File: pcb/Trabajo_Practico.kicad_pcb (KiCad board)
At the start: 2 copper layers, 64 x 110 mm, 49 parts, among them J1 USB_B_Micro, Q1 UMH3N, SW1 RESET, SW2 SW_SPDT, SW3 UP, SW4 DOWN, SW5 LEFT, SW6 RIGHT, SW7 A, SW8 B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

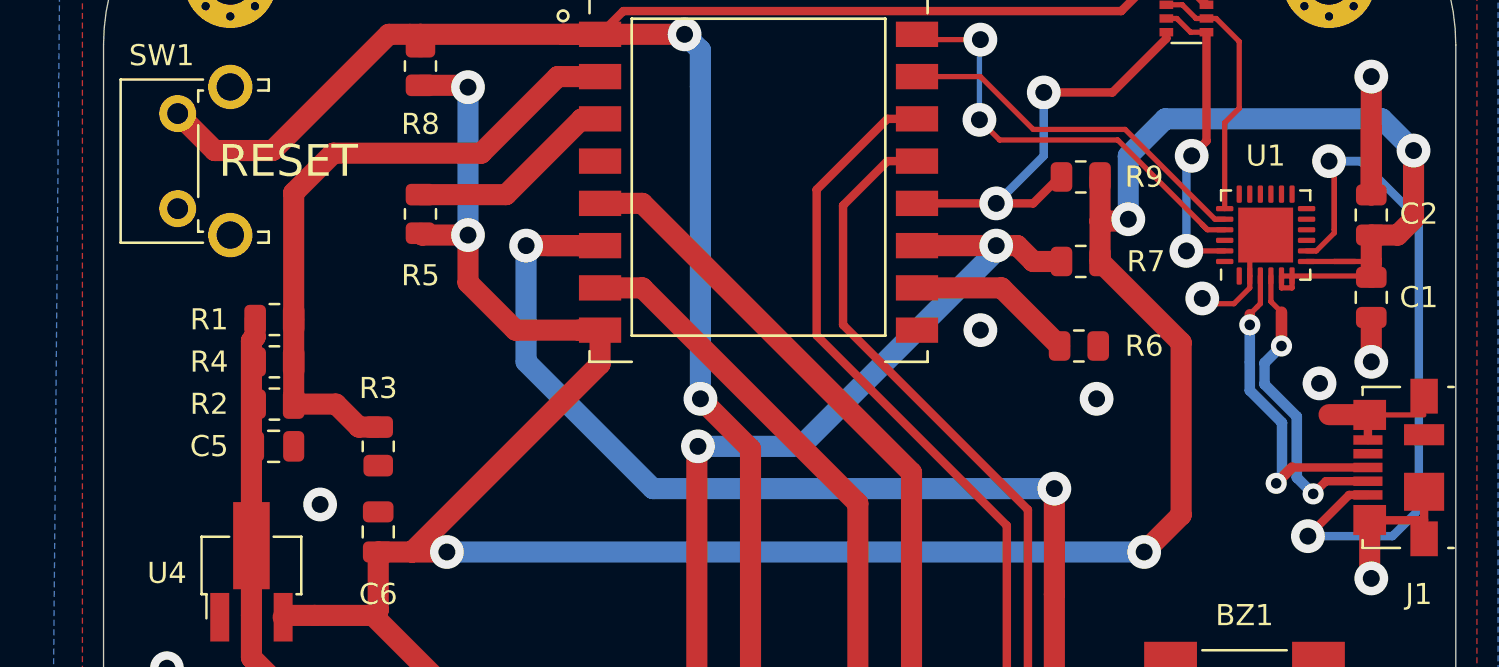
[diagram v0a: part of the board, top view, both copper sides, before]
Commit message: Fix: clearance to 0.25 and values in schematic
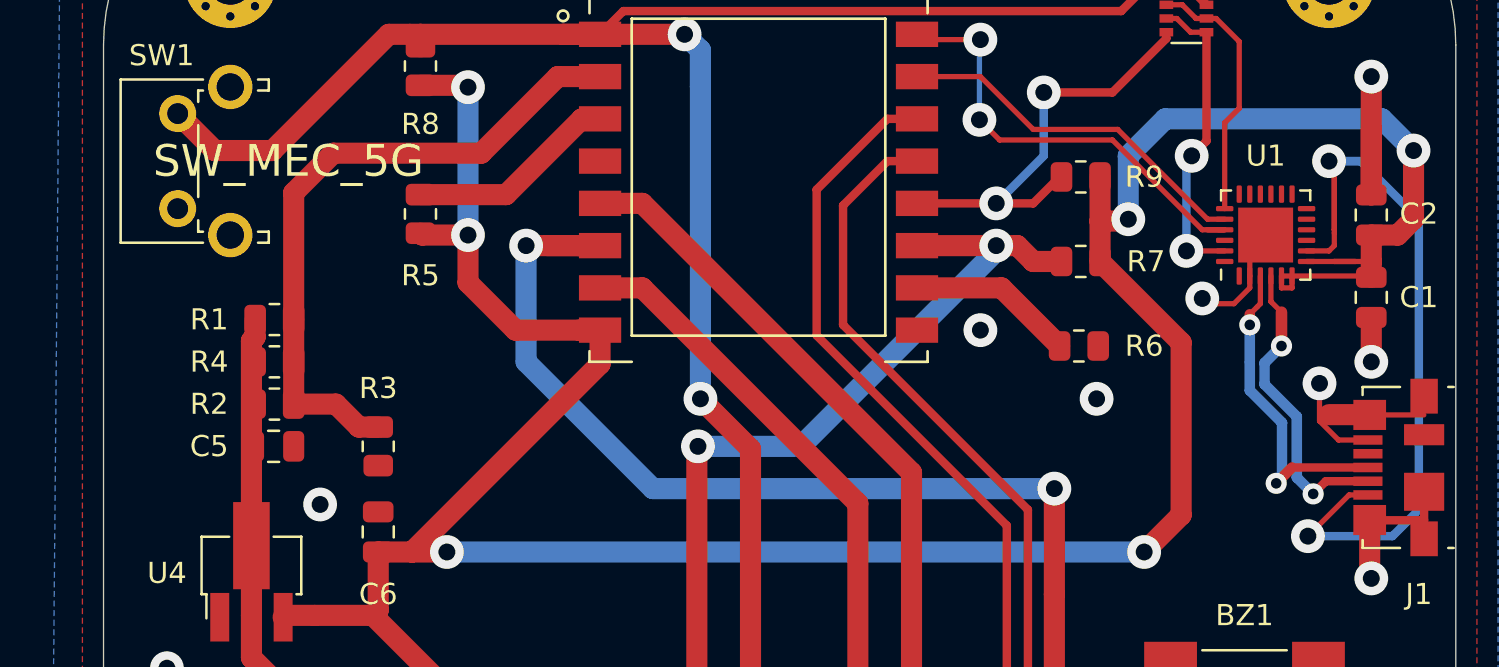
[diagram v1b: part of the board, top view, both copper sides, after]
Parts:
- BZ1: value CMT-8503-85B-SMT-TR -> Buzzer
- DS1: value ST7735_1.44_128x128_SPI -> TFT Display 1.44''
- SW1: value RESET -> SW_MEC_5G
- U1: value CP2104 -> USB2UART
- U3: value PCA9539APW -> GPIO Expander
- U4: value H7650-33PR -> LDO 3.3v 750mA
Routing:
- net GND: track 116.9 -> 120.2 mm
- net /TXD: track 21.0 -> 21.5 mm
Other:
- net class Default: clearance 0.2 -> 0.25
- rule trace_clearance: 0.2 -> 0.25
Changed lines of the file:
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@@
     (thickness 1.6)
     (drawings 37)
-    (tracks 426)
+    (tracks 428)
     (zones 0)
     (modules 49)
@@
     (user_trace_width 0.4)
     (user_trace_width 1)
-    (trace_clearance 0.2)
+    (trace_clearance 0.25)
     (zone_clearance 0.508)
     (zone_45_only no)
@@
   (net 57 /D+)
   (net_class Default "This is the default net class."
-    (clearance 0.2)
+    (clearance 0.25)
     (trace_width 0.4)
     (via_dia 1.6)
@@
       (effects (font (size 1 1) (thickness 0.15)))
     )
-    (fp_text value ST7735_1.44_128x128_SPI (at 10 4 180) (layer F.Fab)
+    (fp_text value "TFT Display 1.44''" (at 10 4 180) (layer F.Fab)
       (effects (font (size 1 1) (thickness 0.15)))
     )
@@
       (effects (font (size 1 1) (thickness 0.15)))
     )
-    (fp_text value RESET (at 2.25 5.24 180) (layer F.SilkS)
+    (fp_text value SW_MEC_5G (at 2.25 5.24 180) (layer F.SilkS)
       (effects (font (size 1.5 1.5) (thickness 0.3)))
     )
@@
       (effects (font (size 1 1) (thickness 0.15)))
     )
-    (fp_text value CMT-8503-85B-SMT-TR (at 0 -6.35 90) (layer F.Fab)
+    (fp_text value Buzzer (at 0 -6.35 90) (layer F.Fab)
       (effects (font (size 1 1) (thickness 0.15)))
     )
@@
     (descr "Micro USB B receptable with flange, bottom-mount, SMD, right-angle (http://www.molex.com/pdm_docs/sd/473460001_sd.pdf)")
     (tags "Micro B USB SMD")
+    (clearance 0.2)
     (attr smd)
     (fp_text reference J1 (at -6 0.95 180) (layer F.SilkS)
@@
     (descr "QFN, 24 Pin (http://ww1.microchip.com/downloads/en/PackagingSpec/00000049BQ.pdf#page=278), generated with kicad-footprint-generator ipc_noLead_generator.py")
     (tags "QFN NoLead")
+    (clearance 0.2)
     (attr smd)
     (fp_text reference U1 (at 3.75 0 180) (layer F.SilkS)
       (effects (font (size 1 1) (thickness 0.15)))
     )
-    (fp_text value CP2104 (at 2.5 7 90) (layer F.Fab)
+    (fp_text value USB2UART (at 2.5 7 90) (layer F.Fab)
       (effects (font (size 1 1) (thickness 0.15)))
     )
@@
       (effects (font (size 1 1) (thickness 0.15)))
     )
-    (fp_text value PCA9539APW (at 0 4.85 90) (layer F.Fab)
+    (fp_text value "GPIO Expander" (at 0 4.85 90) (layer F.Fab)
       (effects (font (size 1 1) (thickness 0.15)))
     )
@@
       (effects (font (size 1 1) (thickness 0.15)))
     )
-    (fp_text value H7650-33PR (at 0.3 3.5 90) (layer F.Fab)
+    (fp_text value "LDO 3.3v 750mA" (at 0.3 3.5 90) (layer F.Fab)
       (effects (font (size 1 1) (thickness 0.15)))
     )
@@
   (via (at 113 78.5) (size 1.6) (drill 0.8) (layers F.Cu B.Cu) (net 2))
   (segment (start 169.84 66.5975) (end 169.925 66.5125) (width 0.4) (layer F.Cu) (net 2))
-  (segment (start 169.84 67.7) (end 169.84 66.5975) (width 0.4) (layer F.Cu) (net 2))
   (segment (start 169.925 66.5125) (end 172.4875 66.5125) (width 0.25) (layer F.Cu) (net 2))
   (segment (start 172.5 70.15) (end 172.5 71.5) (width 0.4) (layer F.Cu) (net 2))
@@
   (via (at 151.5 62.5) (size 1.6) (drill 0.8) (layers F.Cu B.Cu) (net 2))
   (via (at 157 65.75) (size 1.6) (drill 0.8) (layers F.Cu B.Cu) (net 2))
+  (segment (start 169.84 67.7) (end 168.45 67.7) (width 0.25) (layer F.Cu) (net 2))
+  (segment (start 167.55 66.8) (end 167.55 65.02) (width 0.25) (layer F.Cu) (net 2))
+  (segment (start 168.45 67.7) (end 167.55 66.8) (width 0.25) (layer F.Cu) (net 2))
   (segment (start 160.5 85.5) (end 157.75 85.5) (width 1) (layer F.Cu) (net 3))
   (segment (start 157.75 85.5) (end 155 82.75) (width 1) (layer F.Cu) (net 3))
@@
   (segment (start 117 92) (end 117 87) (width 1) (layer F.Cu) (net 11))
   (via (at 167 72.25) (size 1.6) (drill 0.8) (layers F.Cu B.Cu) (net 12))
-  (segment (start 169.84 70.3) (end 168.95 70.3) (width 0.4) (layer F.Cu) (net 12))
-  (segment (start 168.95 70.3) (end 167 72.25) (width 0.4) (layer F.Cu) (net 12))
   (via (at 168 54.5) (size 1.6) (drill 0.8) (layers F.Cu B.Cu) (net 12))
-  (segment (start 167.398022 58.75) (end 168.25 57.898022) (width 0.25) (layer F.Cu) (net 12))
-  (segment (start 166.9375 58.75) (end 167.398022 58.75) (width 0.25) (layer F.Cu) (net 12))
   (segment (start 168.25 54.75) (end 168 54.5) (width 0.25) (layer F.Cu) (net 12))
   (segment (start 168.25 57.75) (end 168.25 54.75) (width 0.25) (layer F.Cu) (net 12))
@@
   (segment (start 171 72.25) (end 172.25 71) (width 0.4) (layer B.Cu) (net 12))
   (segment (start 169.5 54.5) (end 168 54.5) (width 0.4) (layer B.Cu) (net 12))
+  (segment (start 166.9375 58.75) (end 168 58.75) (width 0.25) (layer F.Cu) (net 12))
+  (segment (start 168.25 58.5) (end 168.25 57.898022) (width 0.25) (layer F.Cu) (net 12))
+  (segment (start 168 58.75) (end 168.25 58.5) (width 0.25) (layer F.Cu) (net 12))
+  (segment (start 168.95 70.3) (end 167 72.25) (width 0.25) (layer F.Cu) (net 12))
+  (segment (start 169.84 70.3) (end 168.95 70.3) (width 0.25) (layer F.Cu) (net 12))
   (segment (start 163.0625 56.75) (end 163.0625 52.6875) (width 0.25) (layer F.Cu) (net 14))
   (segment (start 163.0625 52.6875) (end 163.75 52) (width 0.25) (layer F.Cu) (net 14))
@@
   (segment (start 150.875 109.625) (end 149 111.5) (width 0.4) (layer F.Cu) (net 27))
   (segment (start 144.75 113.75) (end 147 111.5) (width 0.4) (layer F.Cu) (net 27))
-  (segment (start 154 53) (end 158.351978 53) (width 0.25) (layer F.Cu) (net 40))
   (segment (start 151.5 50.5) (end 154 53) (width 0.25) (layer F.Cu) (net 40))
-  (segment (start 162.601978 57.25) (end 163.0625 57.25) (width 0.25) (layer F.Cu) (net 40))
-  (segment (start 158.351978 53) (end 162.601978 57.25) (width 0.25) (layer F.Cu) (net 40))
   (segment (start 148.5 50.5) (end 151.5 50.5) (width 0.25) (layer F.Cu) (net 40))
+  (segment (start 163.0625 57.25) (end 162.25 57.25) (width 0.25) (layer F.Cu) (net 40))
+  (segment (start 162.25 57.25) (end 158 53) (width 0.25) (layer F.Cu) (net 40))
+  (segment (start 154 53) (end 158 53) (width 0.25) (layer F.Cu) (net 40))
   (via (at 151.454504 52.545496) (size 1.6) (drill 0.8) (layers F.Cu B.Cu) (net 41))
-  (segment (start 158 53.5) (end 152.409008 53.5) (width 0.25) (layer F.Cu) (net 41))
   (segment (start 152.409008 53.5) (end 151.454504 52.545496) (width 0.25) (layer F.Cu) (net 41))
   (via (at 151.5 48.75) (size 1.6) (drill 0.8) (layers F.Cu B.Cu) (net 41))
@@
   (segment (start 148.75 48.75) (end 148.5 48.5) (width 0.25) (layer F.Cu) (net 41))
   (segment (start 151.5 48.75) (end 148.75 48.75) (width 0.25) (layer F.Cu) (net 41))
-  (segment (start 162.25 57.75) (end 162 57.5) (width 0.25) (layer F.Cu) (net 41))
   (segment (start 163.0625 57.75) (end 162.25 57.75) (width 0.25) (layer F.Cu) (net 41))
-  (segment (start 162.20001 57.70001) (end 162 57.5) (width 0.25) (layer F.Cu) (net 41))
-  (segment (start 162 57.5) (end 158 53.5) (width 0.25) (layer F.Cu) (net 41))
+  (segment (start 162 57.75) (end 157.75 53.5) (width 0.25) (layer F.Cu) (net 41))
+  (segment (start 163.0625 57.75) (end 162 57.75) (width 0.25) (layer F.Cu) (net 41))
+  (segment (start 157.75 53.5) (end 152.409008 53.5) (width 0.25) (layer F.Cu) (net 41))
   (segment (start 147.1 52.5) (end 148.5 52.5) (width 0.4) (layer F.Cu) (net 44))
   (segment (start 149.575 102.6375) (end 149.575 100.576457) (width 0.4) (layer F.Cu) (net 44))
